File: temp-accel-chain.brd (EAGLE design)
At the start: 29.3 x 10.5 mm, 7 parts, among them U1 ADT7420UCPZ-R2

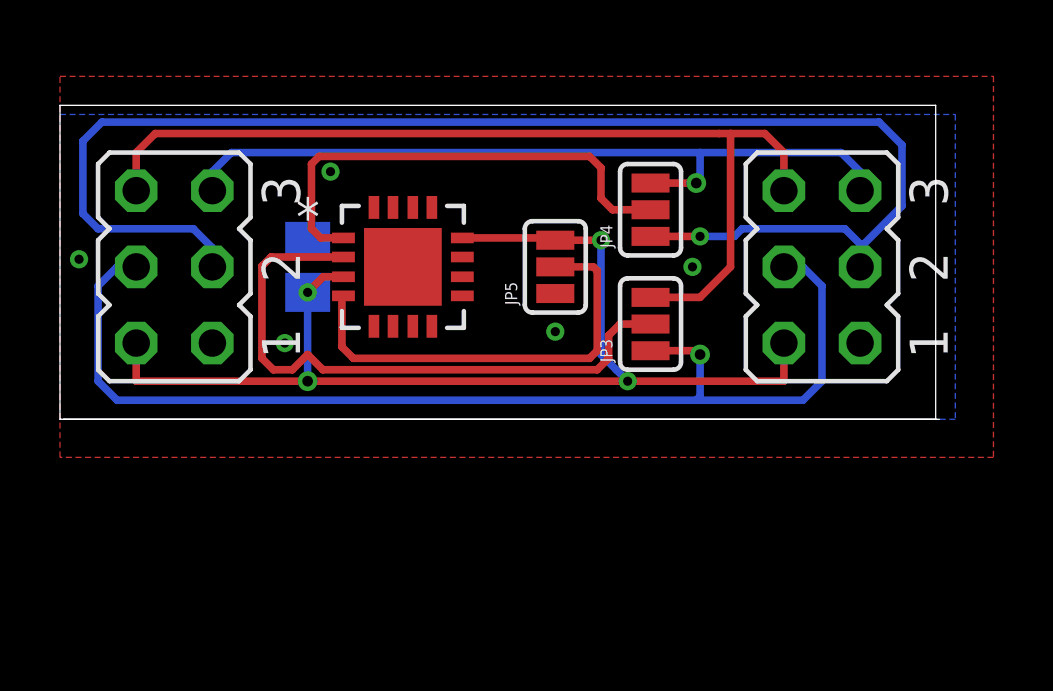
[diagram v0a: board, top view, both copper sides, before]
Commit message: silk screen worked on. drc fixed
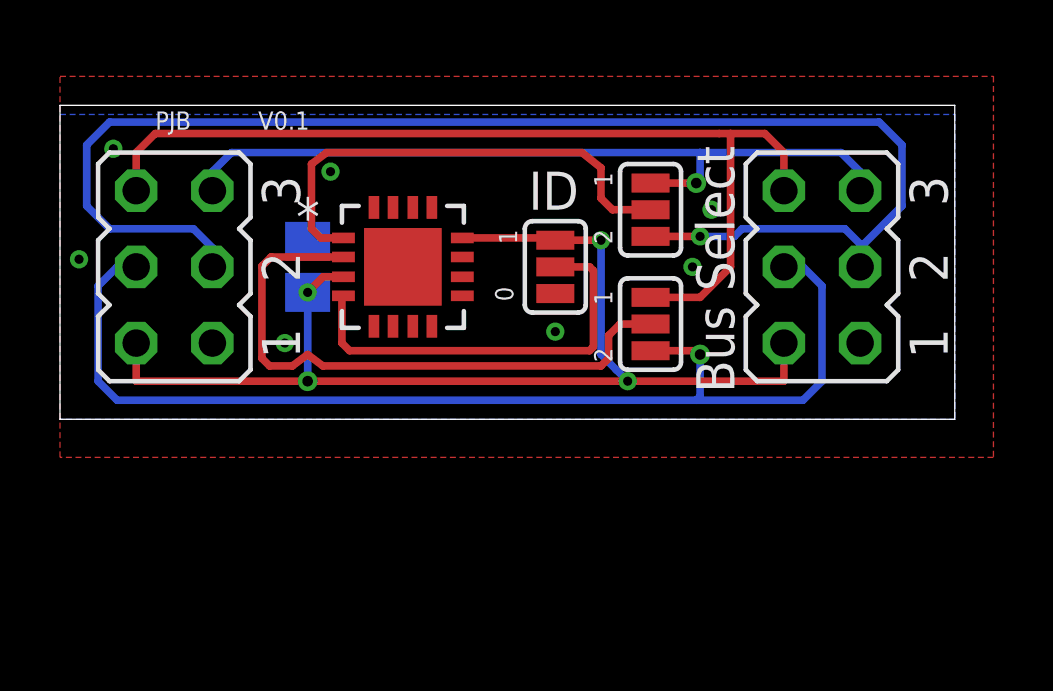
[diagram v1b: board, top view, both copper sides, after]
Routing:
- net ADD: track 14.6 -> 14.0 mm
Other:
- board size 29.3 x 10.5 mm -> 29.8 x 10.5 mm
- board text added: "0"
- board text added: "1"
- board text added: "2"
- board text added: "Bus Select"
- board text added: "ID"
- board text added: "PJB"
- board text added: "V0.1"
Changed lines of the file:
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@@
 <board>
 <plain>
-<wire x1="1.27" y1="0" x2="1.397" y2="0" width="0" layer="20"/>
-<wire x1="1.397" y1="0" x2="30.46" y2="0" width="0" layer="20"/>
-<wire x1="30.46" y1="0" x2="30.46" y2="10.465" width="0" layer="20"/>
-<wire x1="30.46" y1="10.465" x2="1.27" y2="10.465" width="0" layer="20"/>
+<wire x1="1.27" y1="0" x2="31.095" y2="0" width="0" layer="20"/>
+<wire x1="31.095" y1="0" x2="31.095" y2="10.465" width="0" layer="20"/>
+<wire x1="31.095" y1="10.465" x2="1.27" y2="10.465" width="0" layer="20"/>
 <wire x1="1.27" y1="10.465" x2="1.27" y2="0" width="0" layer="20"/>
-<wire x1="1.397" y1="0" x2="30.587" y2="0" width="0" layer="20"/>
+<text x="23.749" y="0.889" size="1.27" layer="25" rot="R90">Bus Select</text>
+<text x="19.685" y="3.81" size="0.6096" layer="25" rot="R90">1</text>
+<text x="19.685" y="7.747" size="0.6096" layer="25" rot="R90">1</text>
+<text x="19.685" y="5.842" size="0.6096" layer="25" rot="R90">2</text>
+<text x="19.685" y="1.905" size="0.6096" layer="25" rot="R90">2</text>
+<text x="16.891" y="6.985" size="1.27" layer="25">ID</text>
+<text x="16.383" y="3.937" size="0.6096" layer="25" rot="R90">0</text>
+<text x="16.51" y="5.842" size="0.6096" layer="25" rot="R90">1</text>
+<text x="4.445" y="9.652" size="0.6096" layer="25">PJB</text>
+<text x="7.874" y="9.652" size="0.6096" layer="25">V0.1</text>
 </plain>
 <attributes>
@@
 <attribute name="VALUE" x="10.922" y="1.651" size="1.27" layer="27" ratio="10" rot="R90"/>
 </element>
-<element name="JP3" library="SparkFun-Passives" package="SJ_3" value="JUMPER-3SMD" x="20.955" y="3.175" smashed="yes" rot="R90">
-<attribute name="NAME" x="19.685" y="1.905" size="0.4064" layer="25" rot="R90"/>
-</element>
+<element name="JP3" library="SparkFun-Passives" package="SJ_3" value="JUMPER-3SMD" x="20.955" y="3.175" smashed="yes" rot="R90"/>
 <element name="JP4" library="SparkFun-Passives" package="SJ_3" value="JUMPER-3SMD" x="20.955" y="6.985" smashed="yes" rot="R90">
-<attribute name="NAME" x="19.685" y="5.715" size="0.4064" layer="25" rot="R90"/>
 <attribute name="VALUE" x="20.955" y="6.8849" size="0.02" layer="27" rot="R90"/>
 </element>
@@
 </element>
 <element name="JP5" library="SparkFun-Passives" package="SJ_3" value="JUMPER-3SMD" x="17.78" y="5.08" smashed="yes" rot="R90">
-<attribute name="NAME" x="16.51" y="3.81" size="0.4064" layer="25" rot="R90"/>
 <attribute name="VALUE" x="17.78" y="4.9799" size="0.02" layer="27" rot="R90"/>
 </element>
@@
 <wire x1="6.35" y1="5.08" x2="6.35" y2="5.715" width="0.254" layer="16"/>
 <wire x1="6.35" y1="5.715" x2="5.715" y2="6.35" width="0.254" layer="16"/>
-<wire x1="5.715" y1="6.35" x2="2.54" y2="6.35" width="0.254" layer="16"/>
-<wire x1="2.54" y1="6.35" x2="2.032" y2="6.858" width="0.254" layer="16"/>
-<wire x1="2.032" y1="6.858" x2="2.032" y2="9.271" width="0.254" layer="16"/>
-<wire x1="2.032" y1="9.271" x2="2.667" y2="9.906" width="0.254" layer="16"/>
-<wire x1="2.667" y1="9.906" x2="28.575" y2="9.906" width="0.254" layer="16"/>
+<wire x1="5.715" y1="6.35" x2="2.921" y2="6.35" width="0.254" layer="16"/>
+<wire x1="2.921" y1="6.35" x2="2.159" y2="7.112" width="0.254" layer="16"/>
+<wire x1="2.159" y1="7.112" x2="2.159" y2="9.144" width="0.254" layer="16"/>
+<wire x1="2.159" y1="9.144" x2="2.921" y2="9.906" width="0.254" layer="16"/>
+<wire x1="2.921" y1="9.906" x2="28.575" y2="9.906" width="0.254" layer="16"/>
 <wire x1="28.575" y1="9.906" x2="29.337" y2="9.144" width="0.254" layer="16"/>
 <wire x1="29.337" y1="9.144" x2="29.337" y2="7.112" width="0.254" layer="16"/>
@@
 <via x="1.905" y="5.334" extent="1-16" drill="0.3048" diameter="0.508"/>
 <via x="10.287" y="8.255" extent="1-16" drill="0.3048" diameter="0.508"/>
+<via x="3.048" y="9.017" extent="1-16" drill="0.3048" diameter="0.508"/>
+<via x="22.987" y="6.985" extent="1-16" drill="0.3048" diameter="0.508"/>
 </signal>
 <signal name="SDA">
@@
 <wire x1="19.939" y1="3.175" x2="19.558" y2="2.794" width="0.254" layer="1"/>
 <wire x1="19.558" y1="2.794" x2="19.558" y2="2.032" width="0.254" layer="1"/>
-<wire x1="19.558" y1="2.032" x2="19.177" y2="1.651" width="0.254" layer="1"/>
-<wire x1="19.177" y1="1.651" x2="10.033" y2="1.651" width="0.254" layer="1"/>
-<wire x1="10.033" y1="1.651" x2="9.525" y2="2.159" width="0.254" layer="1"/>
-<wire x1="9.525" y1="2.159" x2="9.017" y2="1.651" width="0.254" layer="1"/>
-<wire x1="9.017" y1="1.651" x2="8.382" y2="1.651" width="0.254" layer="1"/>
-<wire x1="8.382" y1="1.651" x2="8.001" y2="2.032" width="0.254" layer="1"/>
+<wire x1="19.558" y1="2.032" x2="19.304" y2="1.778" width="0.254" layer="1"/>
+<wire x1="19.304" y1="1.778" x2="10.033" y2="1.778" width="0.254" layer="1"/>
+<wire x1="10.033" y1="1.778" x2="9.525" y2="2.159" width="0.254" layer="1"/>
+<wire x1="9.525" y1="2.159" x2="9.017" y2="1.778" width="0.254" layer="1"/>
+<wire x1="9.017" y1="1.778" x2="8.255" y2="1.778" width="0.254" layer="1"/>
+<wire x1="8.255" y1="1.778" x2="8.001" y2="2.032" width="0.254" layer="1"/>
 <wire x1="8.001" y1="2.032" x2="8.001" y2="5.1054" width="0.254" layer="1"/>
 <wire x1="8.001" y1="5.1054" x2="8.3058" y2="5.4102" width="0.254" layer="1"/>
@@
 <wire x1="9.9568" y1="6.0452" x2="9.652" y2="6.35" width="0.254" layer="1"/>
 <wire x1="9.652" y1="6.35" x2="9.652" y2="8.509" width="0.254" layer="1"/>
-<wire x1="9.652" y1="8.509" x2="9.906" y2="8.763" width="0.254" layer="1"/>
-<wire x1="9.906" y1="8.763" x2="18.923" y2="8.763" width="0.254" layer="1"/>
-<wire x1="18.923" y1="8.763" x2="19.304" y2="8.382" width="0.254" layer="1"/>
+<wire x1="9.652" y1="8.509" x2="10.16" y2="8.89" width="0.254" layer="1"/>
+<wire x1="10.16" y1="8.89" x2="18.669" y2="8.89" width="0.254" layer="1"/>
+<wire x1="18.669" y1="8.89" x2="19.304" y2="8.382" width="0.254" layer="1"/>
 <wire x1="19.304" y1="8.382" x2="19.304" y2="7.366" width="0.254" layer="1"/>
 <wire x1="19.304" y1="7.366" x2="19.685" y2="6.985" width="0.254" layer="1"/>
@@
 <contactref element="U1" pad="4"/>
 <contactref element="JP5" pad="2"/>
-<wire x1="17.78" y1="5.08" x2="19.05" y2="5.08" width="0.254" layer="1"/>
-<wire x1="11.049" y1="2.032" x2="10.668" y2="2.413" width="0.254" layer="1"/>
-<wire x1="10.668" y1="2.413" x2="10.668" y2="4.064" width="0.254" layer="1"/>
+<wire x1="17.78" y1="5.08" x2="18.923" y2="5.08" width="0.254" layer="1"/>
+<wire x1="10.922" y1="2.286" x2="10.668" y2="2.54" width="0.254" layer="1"/>
+<wire x1="10.668" y1="2.54" x2="10.668" y2="4.064" width="0.254" layer="1"/>
 <wire x1="10.668" y1="4.064" x2="10.7188" y2="4.1148" width="0.254" layer="1"/>
-<wire x1="11.049" y1="2.032" x2="18.923" y2="2.032" width="0.254" layer="1"/>
-<wire x1="18.923" y1="2.032" x2="19.177" y2="2.286" width="0.254" layer="1"/>
-<wire x1="19.177" y1="2.286" x2="19.177" y2="4.953" width="0.254" layer="1"/>
-<wire x1="19.177" y1="4.953" x2="19.05" y2="5.08" width="0.254" layer="1"/>
+<wire x1="10.922" y1="2.286" x2="18.923" y2="2.286" width="0.254" layer="1"/>
+<wire x1="18.923" y1="2.286" x2="19.05" y2="2.413" width="0.254" layer="1"/>
+<wire x1="19.05" y1="2.413" x2="19.05" y2="4.953" width="0.254" layer="1"/>
+<wire x1="19.05" y1="4.953" x2="18.923" y2="5.08" width="0.254" layer="1"/>
 </signal>
 </signals>

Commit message: added 10ks to adress lines
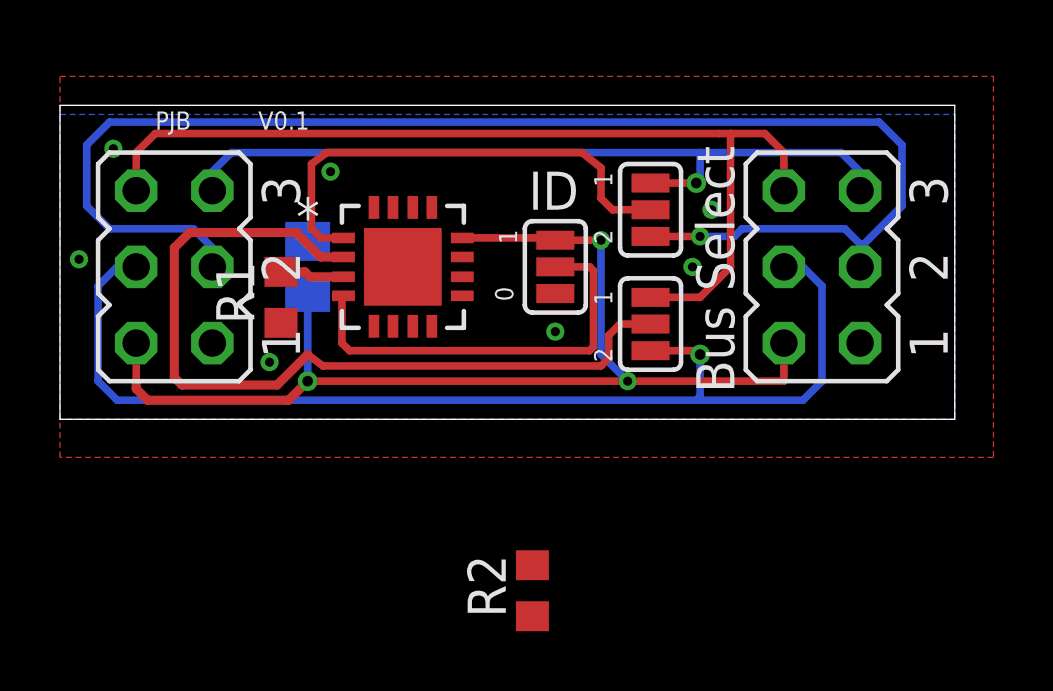
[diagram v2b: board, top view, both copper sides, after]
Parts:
- added R1, R2: 10K, resistor:R0603
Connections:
- new net N$1: R1.2, U1.3
- new net N$3: R2.2, U1.4
- net ADD: now also R2.1; no longer U1.4
- net VCC: now also R1.1; no longer U1.3
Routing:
- net SDA: track 20.3 -> 28.1 mm
- net N$1: track 0.00 -> 2.15 mm
- net VCC: track 38.2 -> 37.5 mm, vias 4 -> 3
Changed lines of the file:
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@@
 <attribute name="VALUE" x="17.78" y="4.9799" size="0.02" layer="27" rot="R90"/>
 </element>
+<element name="R1" library="resistor" package="R0603" value="10K" x="8.636" y="4.064" smashed="yes" rot="R90">
+<attribute name="NAME" x="7.747" y="3.175" size="1.27" layer="25" rot="R90"/>
+</element>
+<element name="R2" library="resistor" package="R0603" value="10K" x="17.018" y="-5.715" rot="R90"/>
 </elements>
 <signals>
@@
 <contactref element="C1" pad="1"/>
 <contactref element="U1" pad="12"/>
-<contactref element="U1" pad="3"/>
 <contactref element="JP5" pad="3"/>
 <wire x1="3.81" y1="2.54" x2="3.81" y2="1.27" width="0.254" layer="1"/>
-<wire x1="3.81" y1="1.27" x2="9.525" y2="1.27" width="0.254" layer="1"/>
 <wire x1="25.4" y1="1.27" x2="25.4" y2="2.54" width="0.254" layer="1"/>
 <via x="9.525" y="1.27" extent="1-16" drill="0.3556" diameter="0.508"/>
 <wire x1="9.525" y1="4.23" x2="9.525" y2="1.27" width="0.254" layer="16"/>
-<via x="9.525" y="4.23" extent="1-16" drill="0.3048" diameter="0.508"/>
 <wire x1="14.6812" y1="6.0452" x2="17.7038" y2="6.0452" width="0.254" layer="1"/>
 <wire x1="17.7038" y1="6.0452" x2="17.78" y2="5.969" width="0.254" layer="1"/>
 <via x="19.304" y="5.969" extent="1-16" drill="0.3048" diameter="0.508"/>
 <wire x1="19.304" y1="5.969" x2="17.78" y2="5.969" width="0.254" layer="1"/>
-<wire x1="10.7188" y1="4.7498" x2="10.0448" y2="4.7498" width="0.254" layer="1"/>
-<wire x1="10.0448" y1="4.7498" x2="9.525" y2="4.23" width="0.254" layer="1"/>
 <wire x1="19.304" y1="5.969" x2="19.304" y2="2.159" width="0.254" layer="16"/>
-<wire x1="19.304" y1="2.159" x2="19.812" y2="1.651" width="0.254" layer="16"/>
+<wire x1="19.304" y1="2.159" x2="20.193" y2="1.27" width="0.254" layer="16"/>
 <wire x1="9.525" y1="1.27" x2="20.193" y2="1.27" width="0.254" layer="1"/>
 <via x="20.193" y="1.27" extent="1-16" drill="0.3048" diameter="0.508"/>
-<wire x1="20.193" y1="1.27" x2="19.812" y2="1.651" width="0.254" layer="16"/>
 <wire x1="20.193" y1="1.27" x2="25.4" y2="1.27" width="0.254" layer="1"/>
+<contactref element="R1" pad="1"/>
+<wire x1="9.525" y1="1.27" x2="8.89" y2="0.635" width="0.3048" layer="1"/>
+<wire x1="8.89" y1="0.635" x2="4.191" y2="0.635" width="0.3048" layer="1"/>
+<wire x1="4.191" y1="0.635" x2="3.81" y2="1.016" width="0.3048" layer="1"/>
+<wire x1="3.81" y1="1.016" x2="3.81" y2="1.27" width="0.3048" layer="1"/>
+<wire x1="9.525" y1="4.23" x2="8.636" y2="3.214" width="0" layer="19" extent="1-16"/>
 </signal>
 <signal name="SCL1">
@@
 <via x="17.78" y="2.921" extent="1-16" drill="0.3048" diameter="0.508"/>
 <via x="22.352" y="5.08" extent="1-16" drill="0.3048" diameter="0.508"/>
-<via x="8.763" y="2.54" extent="1-16" drill="0.3048" diameter="0.508"/>
+<via x="8.255" y="1.905" extent="1-16" drill="0.3048" diameter="0.508"/>
 <via x="1.905" y="5.334" extent="1-16" drill="0.3048" diameter="0.508"/>
 <via x="10.287" y="8.255" extent="1-16" drill="0.3048" diameter="0.508"/>
 <via x="3.048" y="9.017" extent="1-16" drill="0.3048" diameter="0.508"/>
 <via x="22.987" y="6.985" extent="1-16" drill="0.3048" diameter="0.508"/>
+<wire x1="6.35" y1="2.54" x2="1.905" y2="5.334" width="0" layer="19" extent="1-1"/>
 </signal>
 <signal name="SDA">
@@
 <wire x1="19.304" y1="1.778" x2="10.033" y2="1.778" width="0.254" layer="1"/>
 <wire x1="10.033" y1="1.778" x2="9.525" y2="2.159" width="0.254" layer="1"/>
-<wire x1="9.525" y1="2.159" x2="9.017" y2="1.778" width="0.254" layer="1"/>
-<wire x1="9.017" y1="1.778" x2="8.255" y2="1.778" width="0.254" layer="1"/>
-<wire x1="8.255" y1="1.778" x2="8.001" y2="2.032" width="0.254" layer="1"/>
-<wire x1="8.001" y1="2.032" x2="8.001" y2="5.1054" width="0.254" layer="1"/>
-<wire x1="8.001" y1="5.1054" x2="8.3058" y2="5.4102" width="0.254" layer="1"/>
-<wire x1="8.3058" y1="5.4102" x2="10.7188" y2="5.4102" width="0.254" layer="1"/>
+<wire x1="9.525" y1="2.159" x2="8.509" y2="1.143" width="0.3048" layer="1"/>
+<wire x1="8.509" y1="1.143" x2="5.334" y2="1.143" width="0.3048" layer="1"/>
+<wire x1="5.334" y1="1.143" x2="5.08" y2="1.397" width="0.3048" layer="1"/>
+<wire x1="5.08" y1="1.397" x2="5.08" y2="5.715" width="0.3048" layer="1"/>
+<wire x1="5.08" y1="5.715" x2="5.588" y2="6.223" width="0.3048" layer="1"/>
+<wire x1="5.588" y1="6.223" x2="9.144" y2="6.223" width="0.3048" layer="1"/>
+<wire x1="10.7188" y1="5.4102" x2="9.9568" y2="5.4102" width="0.3048" layer="1"/>
+<wire x1="9.9568" y1="5.4102" x2="9.144" y2="6.223" width="0.3048" layer="1"/>
 </signal>
 <signal name="SCL">
@@
 </signal>
 <signal name="ADD">
-<contactref element="U1" pad="4"/>
 <contactref element="JP5" pad="2"/>
 <wire x1="17.78" y1="5.08" x2="18.923" y2="5.08" width="0.254" layer="1"/>
 <wire x1="10.922" y1="2.286" x2="10.668" y2="2.54" width="0.254" layer="1"/>
 <wire x1="10.668" y1="2.54" x2="10.668" y2="4.064" width="0.254" layer="1"/>
-<wire x1="10.668" y1="4.064" x2="10.7188" y2="4.1148" width="0.254" layer="1"/>
 <wire x1="10.922" y1="2.286" x2="18.923" y2="2.286" width="0.254" layer="1"/>
 <wire x1="18.923" y1="2.286" x2="19.05" y2="2.413" width="0.254" layer="1"/>
 <wire x1="19.05" y1="2.413" x2="19.05" y2="4.953" width="0.254" layer="1"/>
 <wire x1="19.05" y1="4.953" x2="18.923" y2="5.08" width="0.254" layer="1"/>
+<contactref element="R2" pad="1"/>
+<wire x1="17.018" y1="-6.565" x2="18.923" y2="2.286" width="0" layer="19" extent="1-1"/>
+</signal>
+<signal name="N$1">
+<contactref element="U1" pad="3"/>
+<contactref element="R1" pad="2"/>
+<wire x1="8.636" y1="4.914" x2="9.437" y2="4.914" width="0.3048" layer="1"/>
+<wire x1="9.437" y1="4.914" x2="9.6012" y2="4.7498" width="0.3048" layer="1"/>
+<wire x1="9.6012" y1="4.7498" x2="10.7188" y2="4.7498" width="0.3048" layer="1"/>
+</signal>
+<signal name="N$3">
+<contactref element="R2" pad="2"/>
+<contactref element="U1" pad="4"/>
+<wire x1="10.7188" y1="4.1148" x2="17.018" y2="-4.865" width="0" layer="19" extent="1-1"/>
 </signal>
 </signals>
